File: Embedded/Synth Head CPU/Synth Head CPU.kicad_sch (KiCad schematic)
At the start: 0 parts

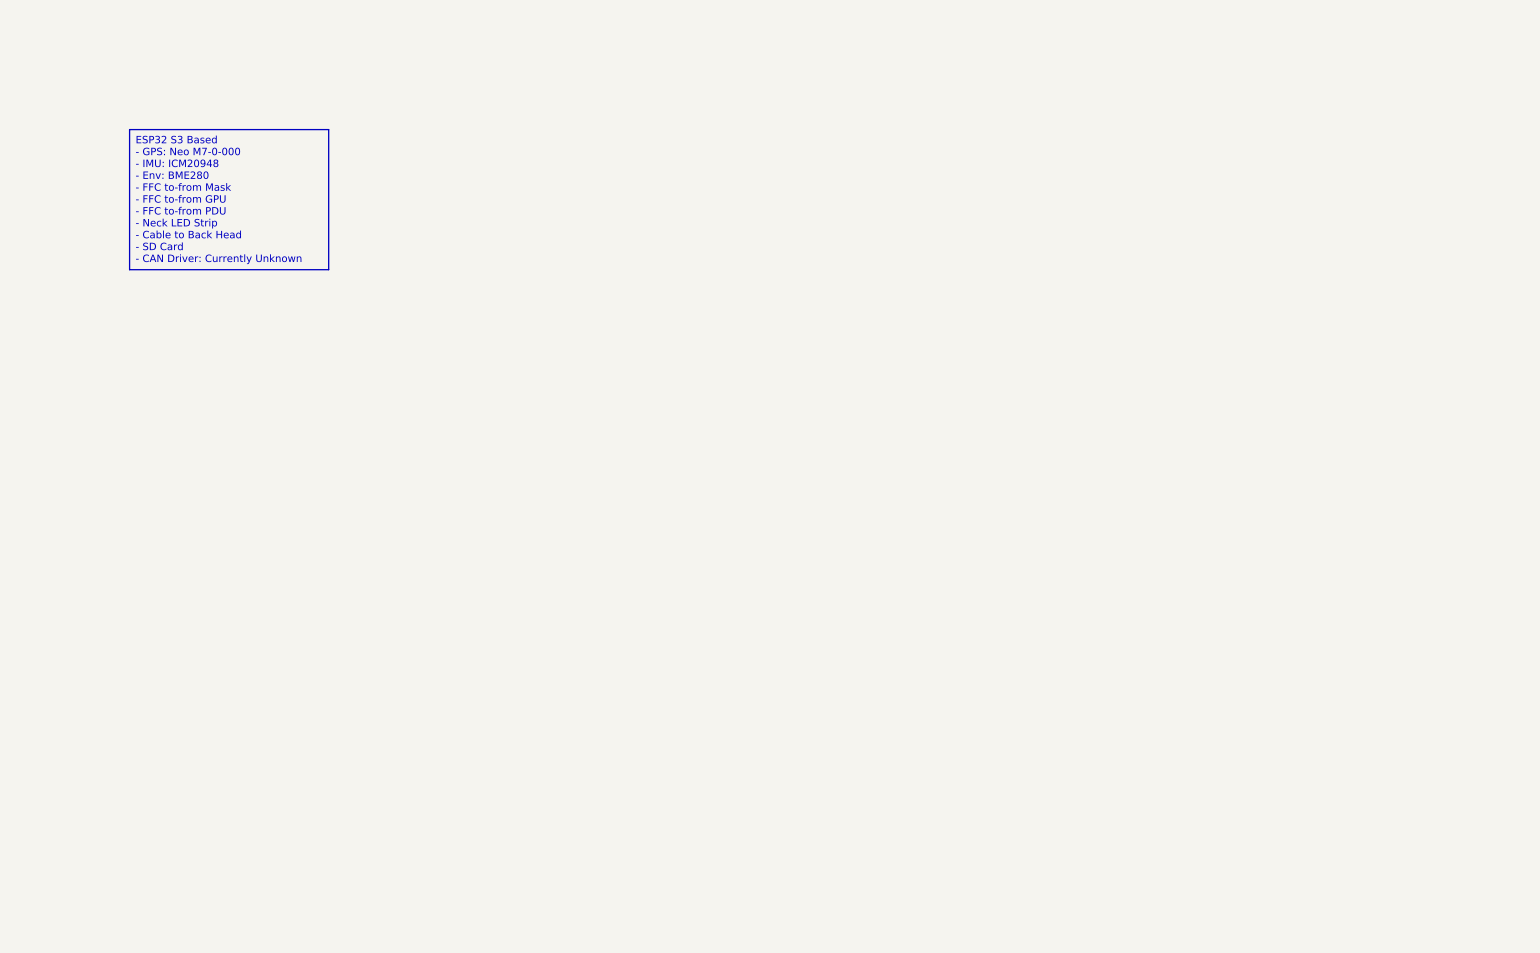
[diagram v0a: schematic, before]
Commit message: Some Sensors Added to the GPU and CPU
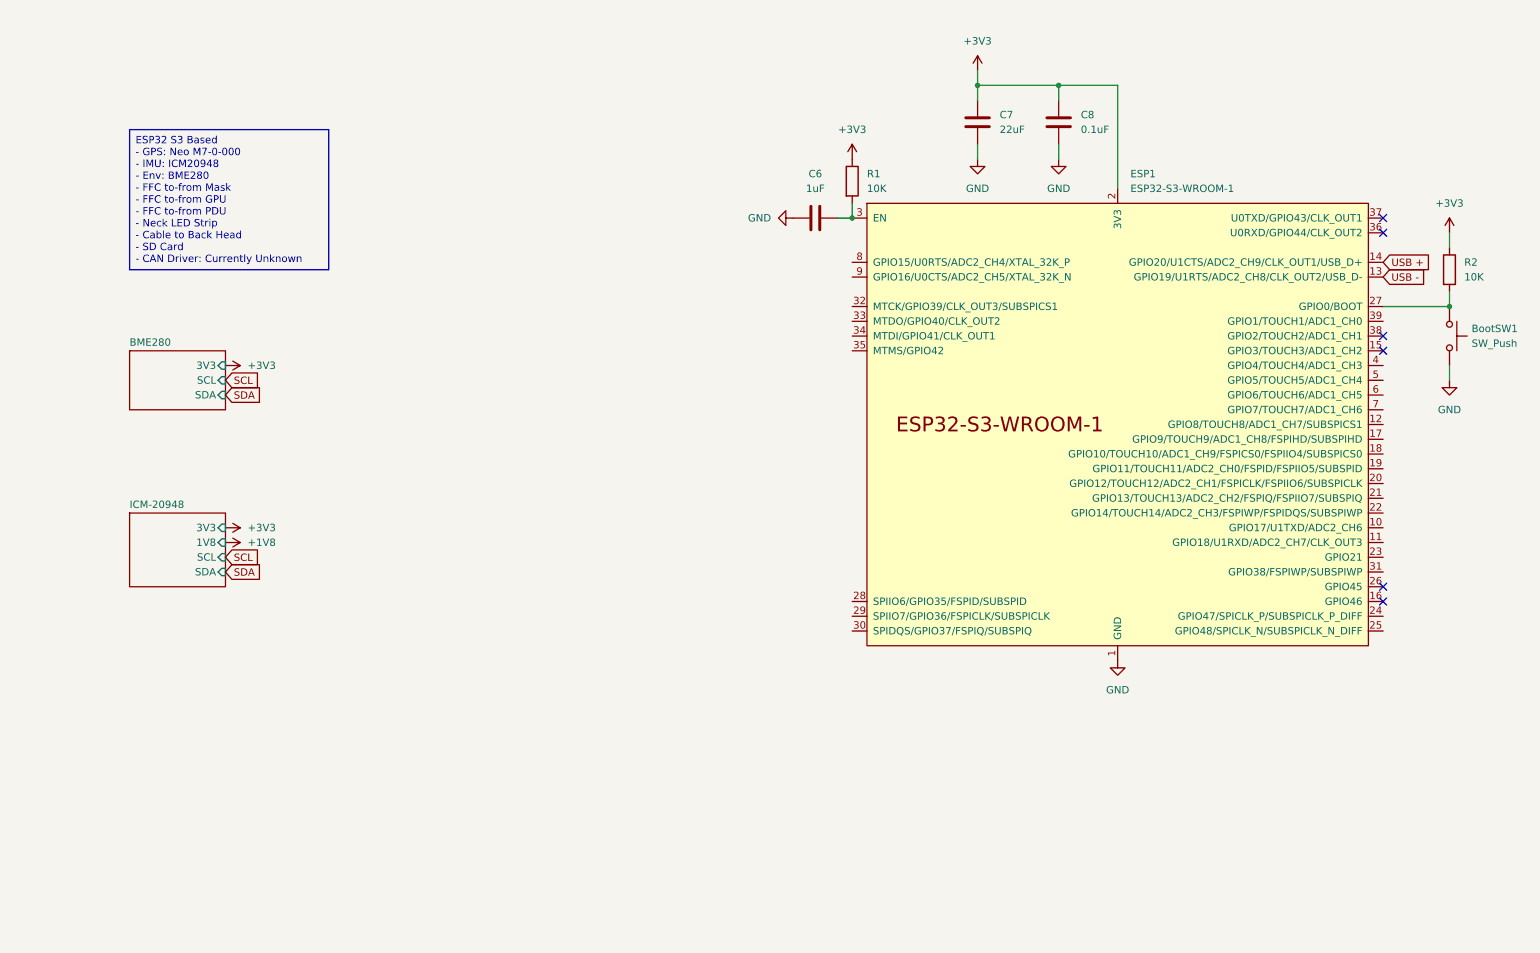
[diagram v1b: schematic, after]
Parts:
- added BootSW1: SW_Push, Button-R-667843:Button-R-667843, symbol Switch:SW_Push
- added C6: 1uF, Capacitor_SMD:C_0603_1608Metric, symbol Device:C
- added C7: 22uF, Capacitor_SMD:C_0603_1608Metric_Pad1.08x0.95mm_HandSolder, symbol Device:C
- added C8: 0.1uF, Capacitor_SMD:C_0603_1608Metric, symbol Device:C
- added ESP1: ESP32-S3-WROOM-1, PCM_Espressif:ESP32-S3-WROOM-1U, symbol PCM_Espressif:ESP32-S3-WROOM-1
- added R1, R2: 10K, Resistor_SMD:R_0603_1608Metric, symbol Device:R
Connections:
- new net: BootSW1.1, ESP1.27 (GPIO0/BOOT), R2.2
- new net: C6.2, ESP1.3 (EN), R1.2
- new net +3V3: C7.1, C8.1, ESP1.2 (3V3), R1.1, R2.1
- new net GND: BootSW1.2, C6.1, C7.2, C8.2, ESP1.1 (GND), ESP1.40 (GND), ESP1.41 (GND)
- new net USB +: ESP1.14 (GPIO20/U1CTS/ADC2_CH9/CLK_OUT1/USB_D+)
- new net USB -: ESP1.13 (GPIO19/U1RTS/ADC2_CH8/CLK_OUT2/USB_D-)
- no-connect marks 0 -> 6
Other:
- added sheet BME280 (BME280.kicad_sch)
- added sheet ICM-20948 (ICM20948.kicad_sch)

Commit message: Majority of the pins for the Mask Board & Snoot Added
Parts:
- ESP1: footprint PCM_Espressif:ESP32-S3-WROOM-1U -> PCM_Espressif:ESP32-S3-WROOM-1
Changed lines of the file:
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@@
 			)
 		)
-		(property "Footprint" "PCM_Espressif:ESP32-S3-WROOM-1U"
+		(property "Footprint" "PCM_Espressif:ESP32-S3-WROOM-1"
 			(at 210.82 137.16 0)
 			(effects

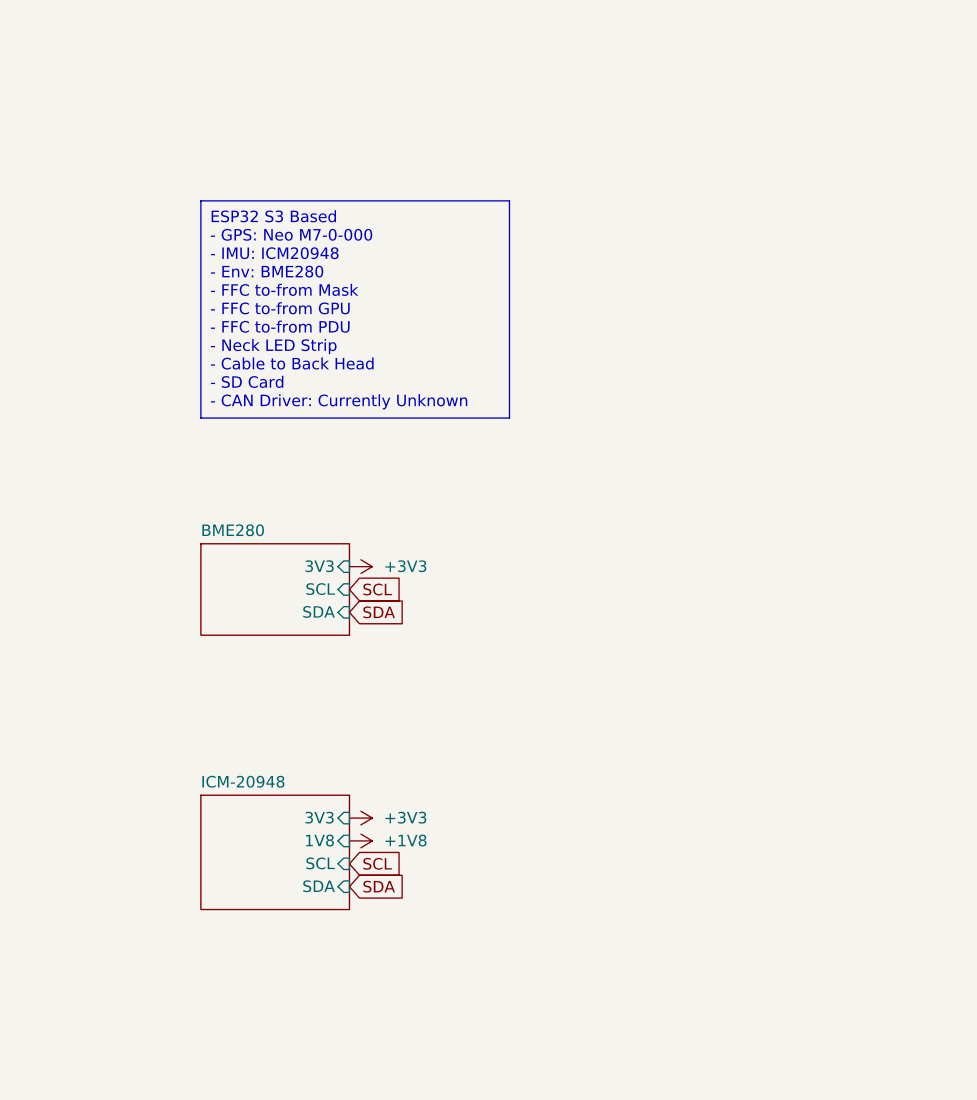
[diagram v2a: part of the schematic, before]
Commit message: CPU Power & USB C Port Added
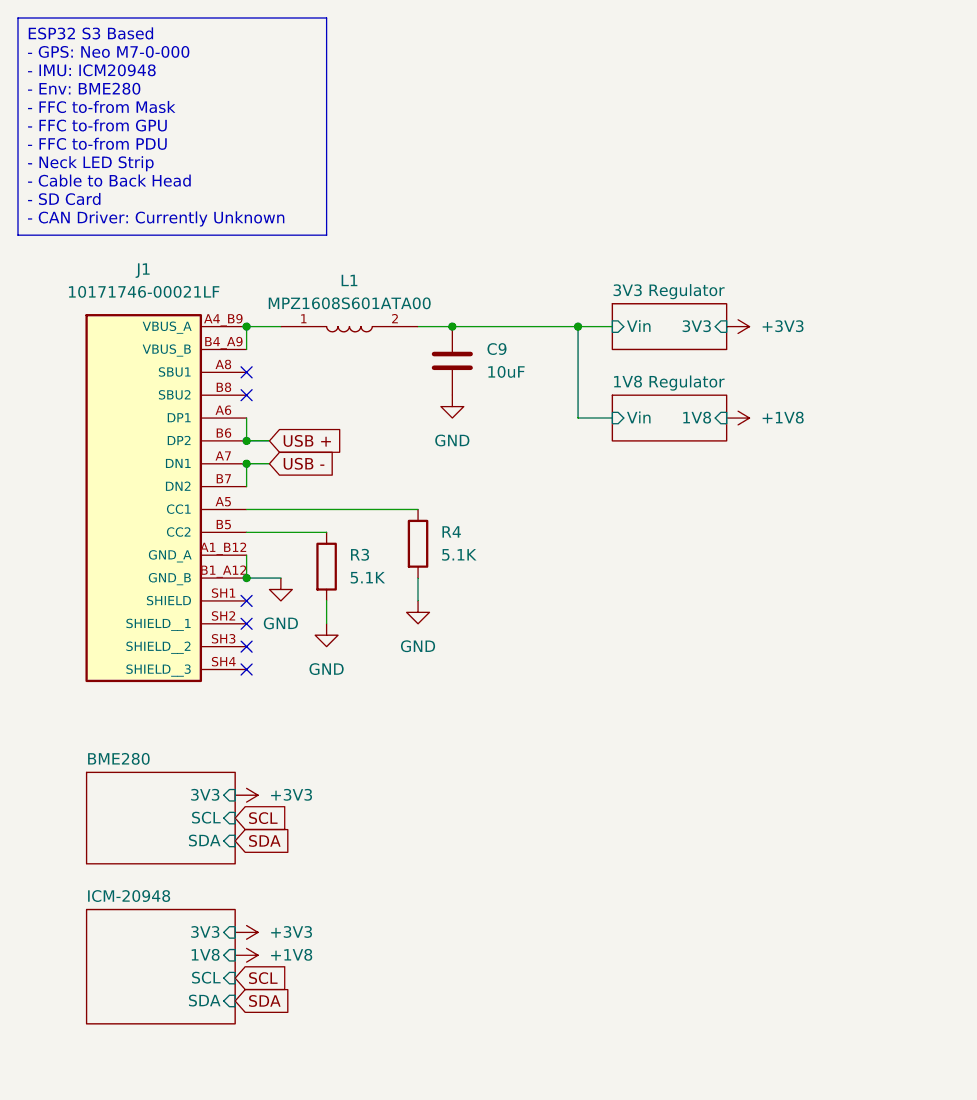
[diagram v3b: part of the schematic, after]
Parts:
- added C9: 10uF, Capacitor_SMD:C_0603_1608Metric, symbol Device:C
- added J1: 10171746-00021LF, USBC_10171746_00021LF:AMPHENOL_10171746-00021LF, symbol USBC_10171746_00021LF:10171746-00021LF
- added L1: MPZ1608S601ATA00, Ferrite_Bead_MPZ1608S601ATA00:INDC1608X95N, symbol Ferrite_Bead_MPZ1608S601ATA00:MPZ1608S601ATA00
- added R3, R4: 5.1K, Resistor_SMD:R_0603_1608Metric, symbol Device:R
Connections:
- net GND: now also C9.2, J1.A1_B12 (GND_A), J1.B1_A12 (GND_B), R3.2, R4.2
- net USB +: now also J1.A6 (DP1), J1.B6 (DP2)
- net USB -: now also J1.A7 (DN1), J1.B7 (DN2)
- new net: J1.A4_B9 (VBUS_A), J1.B4_A9 (VBUS_B), L1.1
- new net: J1.A5 (CC1), R4.1
- new net: J1.B5 (CC2), R3.1
- new net 1V8 Regulator/Vin: C9.1, L1.2
- no-connect marks 6 -> 12
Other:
- added sheet 1V8 Regulator (1V8 Reg.kicad_sch)
- added sheet 3V3 Regulator (3V3 Reg.kicad_sch)

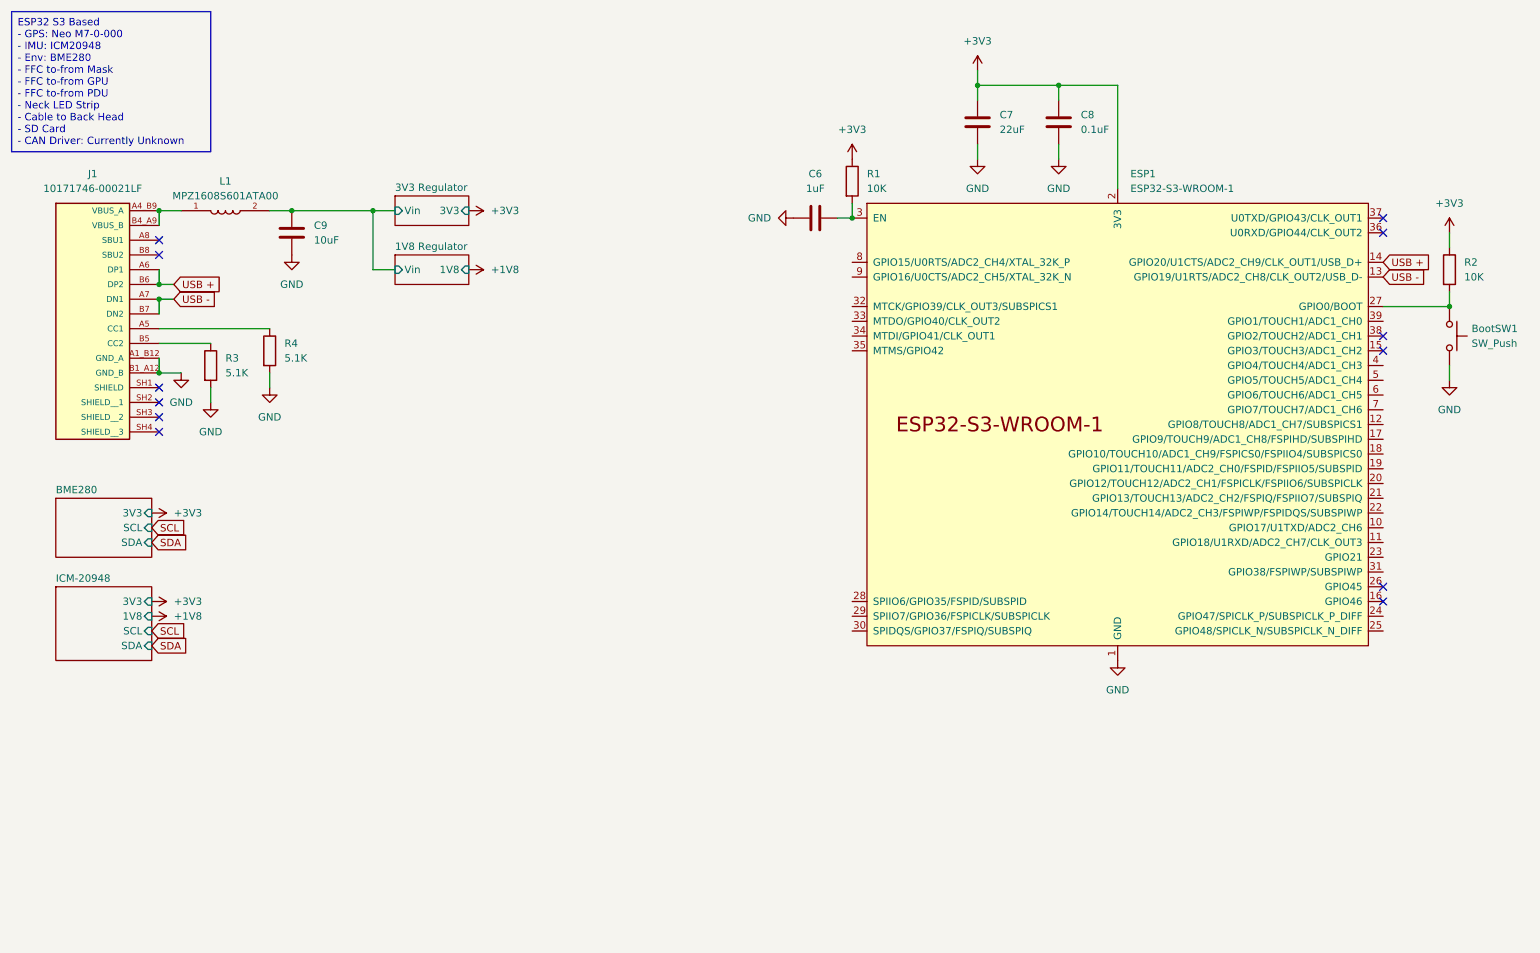
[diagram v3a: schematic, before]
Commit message: CPU FFC Ports Added
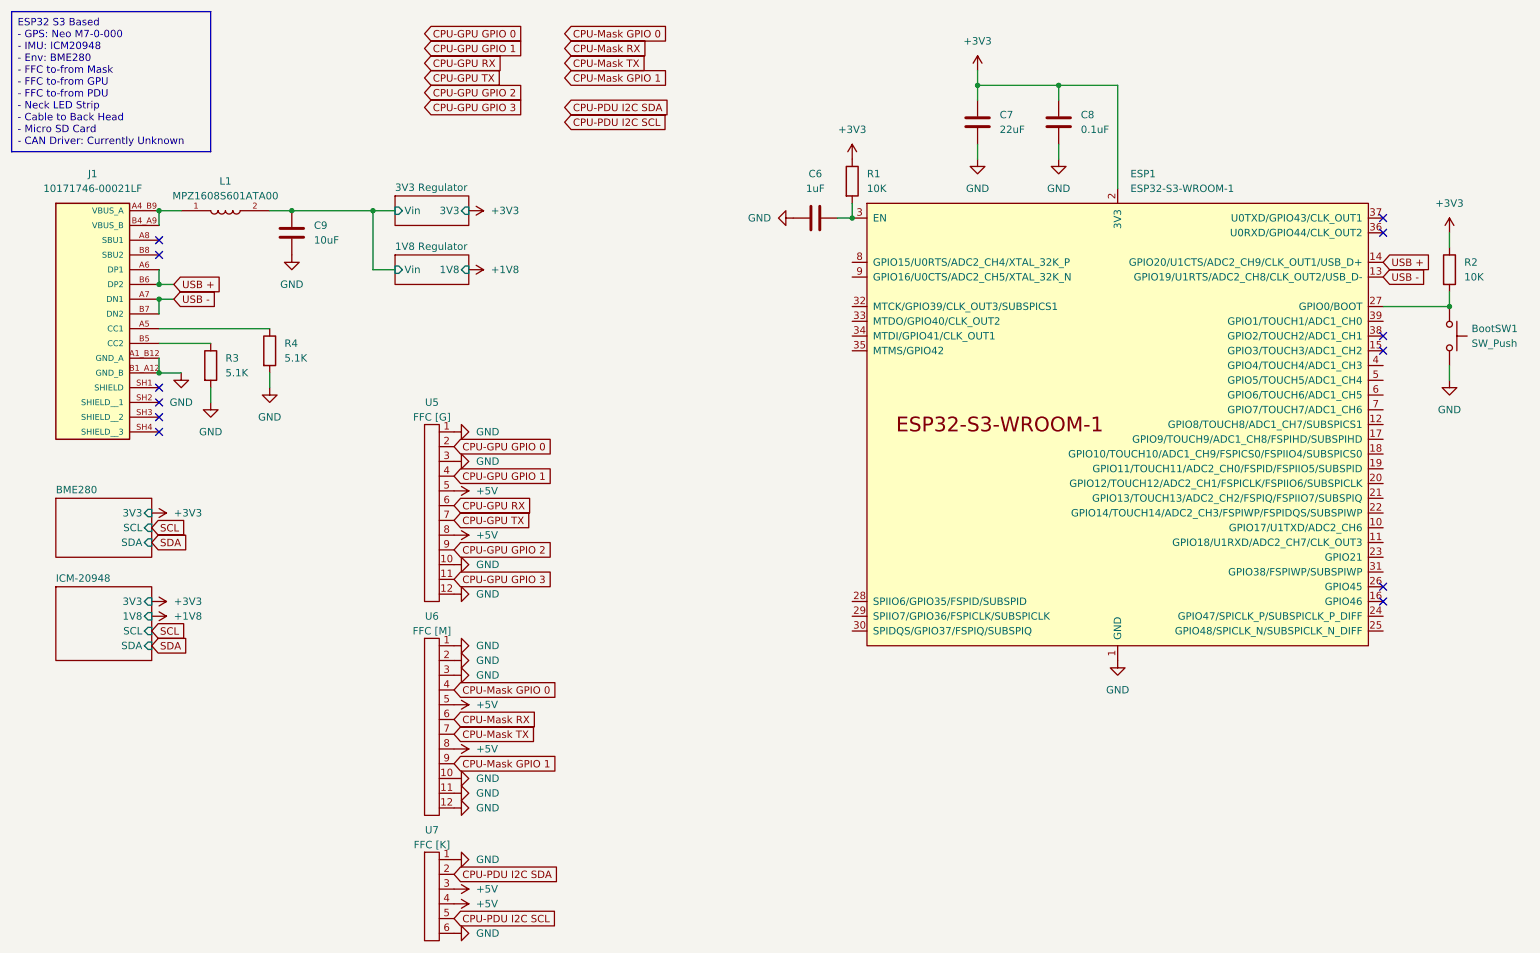
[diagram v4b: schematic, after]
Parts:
- added U5: FFC [G], FFC_Connector:FFC Aliexpress 0.5mm 12P, symbol FCC_Connector:FFC_12P
- added U6: FFC [M], FFC_Connector:FFC Aliexpress 0.5mm 12P, symbol FCC_Connector:FFC_12P
- added U7: FFC [K], FFC_Connector:FFC Aliexpress 0.5mm 6P, symbol FCC_Connector:FFC_6P
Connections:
- net GND: now also U5.1, U5.10, U5.12, U5.3, U6.1, U6.10, U6.11, U6.12, U6.2, U6.3, U7.1, U7.6
- new net +5V: U5.5, U5.8, U6.5, U6.8, U7.3, U7.4
- new net CPU-GPU GPIO 0: U5.2
- new net CPU-GPU GPIO 1: U5.4
- new net CPU-GPU GPIO 2: U5.9
- new net CPU-GPU GPIO 3: U5.11
- new net CPU-GPU RX: U5.6
- new net CPU-GPU TX: U5.7
- new net CPU-Mask GPIO 0: U6.4
- new net CPU-Mask GPIO 1: U6.9
- new net CPU-Mask RX: U6.6
- new net CPU-Mask TX: U6.7
- new net CPU-PDU I2C SCL: U7.5
- new net CPU-PDU I2C SDA: U7.2
